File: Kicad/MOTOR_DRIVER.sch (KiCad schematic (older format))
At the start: 8 parts, among them J1 CONN_MOTOR, U1 SHFTREG_H, U2 LV8727

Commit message: 
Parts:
- removed L1: __BATTERYBARLUG, ~, symbol __BATTERYBARLUG
- added L1: LUG, ~, symbol LUG
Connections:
- net labels added: CS, FR, SDIN, SDOUT, STEP, VREF
- net labels removed: MOTOR_CS, MOTOR_FR, MOTOR_SDIN, MOTOR_SDOUT, MOTOR_STEP, MOTOR_VREF

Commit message: All wired. ERC passes with no errors. Might be good to go.
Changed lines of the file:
@@
 $Descr A4 11693 8268
 encoding utf-8
-Sheet 2 15
+Sheet 14 15
 Title ""
-Date "7 jun 2014"
+Date "8 jun 2014"
 Rev ""
 Comp ""
@@
 P 5650 2400
 AR Path="/5387F799/53880645" Ref="U2"  Part="1"
-AR Path="/5393B696/53880645" Ref="U12"  Part="1"
-AR Path="/5393E24C/53880645" Ref="U14"  Part="1"
-AR Path="/5393E5B4/53880645" Ref="U16"  Part="1"
-F 0 "U2" V 4300 2600 60  0000 C CNN
+AR Path="/5393B696/53880645" Ref="U8"  Part="1"
+AR Path="/5393E24C/53880645" Ref="U10"  Part="1"
+AR Path="/5393E5B4/53880645" Ref="U12"  Part="1"
+F 0 "U12" V 4300 2600 60  0000 C CNN
 F 1 "LV8727" V 7050 2600 60  0000 C CNN
 F 2 "~" H 5650 2400 60  0000 C CNN
@@
 P 4250 5150
 AR Path="/5387F799/53880692" Ref="U1"  Part="1"
-AR Path="/5393B696/53880692" Ref="U11"  Part="1"
-AR Path="/5393E24C/53880692" Ref="U13"  Part="1"
-AR Path="/5393E5B4/53880692" Ref="U15"  Part="1"
-F 0 "U1" H 4250 5700 60  0000 C CNN
+AR Path="/5393B696/53880692" Ref="U7"  Part="1"
+AR Path="/5393E24C/53880692" Ref="U9"  Part="1"
+AR Path="/5393E5B4/53880692" Ref="U11"  Part="1"
+F 0 "U11" H 4250 5700 60  0000 C CNN
 F 1 "SHFTREG_H" H 4250 4600 60  0000 C CNN
 F 2 "~" V 4000 5250 60  0000 C CNN
@@
 P 6750 2950
 AR Path="/5387F799/538A3F7A" Ref="R2"  Part="1"
-AR Path="/5393B696/538A3F7A" Ref="R16"  Part="1"
-AR Path="/5393E24C/538A3F7A" Ref="R18"  Part="1"
-AR Path="/5393E5B4/538A3F7A" Ref="R20"  Part="1"
-F 0 "R2" V 6830 2950 40  0000 C CNN
+AR Path="/5393B696/538A3F7A" Ref="R10"  Part="1"
+AR Path="/5393E24C/538A3F7A" Ref="R12"  Part="1"
+AR Path="/5393E5B4/538A3F7A" Ref="R14"  Part="1"
+F 0 "R14" V 6830 2950 40  0000 C CNN
 F 1 "0.1" V 6757 2951 40  0000 C CNN
 F 2 "~" V 6680 2950 30  0000 C CNN
@@
 P 4550 2950
 AR Path="/5387F799/538A3F87" Ref="R1"  Part="1"
-AR Path="/5393B696/538A3F87" Ref="R15"  Part="1"
-AR Path="/5393E24C/538A3F87" Ref="R17"  Part="1"
-AR Path="/5393E5B4/538A3F87" Ref="R19"  Part="1"
-F 0 "R1" V 4630 2950 40  0000 C CNN
+AR Path="/5393B696/538A3F87" Ref="R9"  Part="1"
+AR Path="/5393E24C/538A3F87" Ref="R11"  Part="1"
+AR Path="/5393E5B4/538A3F87" Ref="R13"  Part="1"
+F 0 "R13" V 4630 2950 40  0000 C CNN
 F 1 "0.1" V 4557 2951 40  0000 C CNN
 F 2 "~" V 4480 2950 30  0000 C CNN
@@
 AR Path="/5393E24C/538A3FA9" Ref="C5"  Part="1"
 AR Path="/5393E5B4/538A3FA9" Ref="C7"  Part="1"
-F 0 "C1" H 4850 4450 40  0000 L CNN
+F 0 "C7" H 4850 4450 40  0000 L CNN
 F 1 "1000u" H 4856 4265 40  0000 L CNN
 F 2 "~" H 4888 4200 30  0000 C CNN
@@
 P 4850 4600
 AR Path="/5387F799/538A3FB8" Ref="#PWR07"  Part="1"
-AR Path="/5393B696/538A3FB8" Ref="#PWR057"  Part="1"
-AR Path="/5393E24C/538A3FB8" Ref="#PWR066"  Part="1"
-AR Path="/5393E5B4/538A3FB8" Ref="#PWR075"  Part="1"
-F 0 "#PWR07" H 4850 4600 30  0001 C CNN
+AR Path="/5393B696/538A3FB8" Ref="#PWR050"  Part="1"
+AR Path="/5393E24C/538A3FB8" Ref="#PWR059"  Part="1"
+AR Path="/5393E5B4/538A3FB8" Ref="#PWR068"  Part="1"
+F 0 "#PWR068" H 4850 4600 30  0001 C CNN
 F 1 "GND" H 4850 4530 30  0001 C CNN
 F 2 "" H 4850 4600 60  0000 C CNN
@@
 P 6350 2750
 AR Path="/5387F799/538A3FEF" Ref="#PWR08"  Part="1"
-AR Path="/5393B696/538A3FEF" Ref="#PWR058"  Part="1"
-AR Path="/5393E24C/538A3FEF" Ref="#PWR067"  Part="1"
-AR Path="/5393E5B4/538A3FEF" Ref="#PWR076"  Part="1"
-F 0 "#PWR08" H 6350 2750 30  0001 C CNN
+AR Path="/5393B696/538A3FEF" Ref="#PWR051"  Part="1"
+AR Path="/5393E24C/538A3FEF" Ref="#PWR060"  Part="1"
+AR Path="/5393E5B4/538A3FEF" Ref="#PWR069"  Part="1"
+F 0 "#PWR069" H 6350 2750 30  0001 C CNN
 F 1 "GND" H 6350 2680 30  0001 C CNN
 F 2 "" H 6350 2750 60  0000 C CNN
@@
 P 6650 2750
 AR Path="/5387F799/538A3FF5" Ref="#PWR09"  Part="1"
-AR Path="/5393B696/538A3FF5" Ref="#PWR059"  Part="1"
-AR Path="/5393E24C/538A3FF5" Ref="#PWR068"  Part="1"
-AR Path="/5393E5B4/538A3FF5" Ref="#PWR077"  Part="1"
-F 0 "#PWR09" H 6650 2750 30  0001 C CNN
+AR Path="/5393B696/538A3FF5" Ref="#PWR052"  Part="1"
+AR Path="/5393E24C/538A3FF5" Ref="#PWR061"  Part="1"
+AR Path="/5393E5B4/538A3FF5" Ref="#PWR070"  Part="1"
+F 0 "#PWR070" H 6650 2750 30  0001 C CNN
 F 1 "GND" H 6650 2680 30  0001 C CNN
 F 2 "" H 6650 2750 60  0000 C CNN
@@
 P 4650 2750
 AR Path="/5387F799/538A3FFB" Ref="#PWR010"  Part="1"
-AR Path="/5393B696/538A3FFB" Ref="#PWR060"  Part="1"
-AR Path="/5393E24C/538A3FFB" Ref="#PWR069"  Part="1"
-AR Path="/5393E5B4/538A3FFB" Ref="#PWR078"  Part="1"
-F 0 "#PWR010" H 4650 2750 30  0001 C CNN
+AR Path="/5393B696/538A3FFB" Ref="#PWR053"  Part="1"
+AR Path="/5393E24C/538A3FFB" Ref="#PWR062"  Part="1"
+AR Path="/5393E5B4/538A3FFB" Ref="#PWR071"  Part="1"
+F 0 "#PWR071" H 4650 2750 30  0001 C CNN
 F 1 "GND" H 4650 2680 30  0001 C CNN
 F 2 "" H 4650 2750 60  0000 C CNN
@@
 P 4550 3250
 AR Path="/5387F799/538A4FB3" Ref="#PWR011"  Part="1"
-AR Path="/5393B696/538A4FB3" Ref="#PWR061"  Part="1"
-AR Path="/5393E24C/538A4FB3" Ref="#PWR070"  Part="1"
-AR Path="/5393E5B4/538A4FB3" Ref="#PWR079"  Part="1"
-F 0 "#PWR011" H 4550 3250 30  0001 C CNN
+AR Path="/5393B696/538A4FB3" Ref="#PWR054"  Part="1"
+AR Path="/5393E24C/538A4FB3" Ref="#PWR063"  Part="1"
+AR Path="/5393E5B4/538A4FB3" Ref="#PWR072"  Part="1"
+F 0 "#PWR072" H 4550 3250 30  0001 C CNN
 F 1 "GND" H 4550 3180 30  0001 C CNN
 F 2 "" H 4550 3250 60  0000 C CNN
@@
 P 6750 3250
 AR Path="/5387F799/538A4FB9" Ref="#PWR012"  Part="1"
-AR Path="/5393B696/538A4FB9" Ref="#PWR062"  Part="1"
-AR Path="/5393E24C/538A4FB9" Ref="#PWR071"  Part="1"
-AR Path="/5393E5B4/538A4FB9" Ref="#PWR080"  Part="1"
-F 0 "#PWR012" H 6750 3250 30  0001 C CNN
+AR Path="/5393B696/538A4FB9" Ref="#PWR055"  Part="1"
+AR Path="/5393E24C/538A4FB9" Ref="#PWR064"  Part="1"
+AR Path="/5393E5B4/538A4FB9" Ref="#PWR073"  Part="1"
+F 0 "#PWR073" H 6750 3250 30  0001 C CNN
 F 1 "GND" H 6750 3180 30  0001 C CNN
 F 2 "" H 6750 3250 60  0000 C CNN
@@
 AR Path="/5393E24C/538A522E" Ref="C6"  Part="1"
 AR Path="/5393E5B4/538A522E" Ref="C8"  Part="1"
-F 0 "C2" H 5800 3100 40  0000 L CNN
+F 0 "C8" H 5800 3100 40  0000 L CNN
 F 1 "180p" H 5806 2915 40  0000 L CNN
 F 2 "~" H 5838 2850 30  0000 C CNN
@@
 P 5800 3250
 AR Path="/5387F799/538A5251" Ref="#PWR013"  Part="1"
-AR Path="/5393B696/538A5251" Ref="#PWR063"  Part="1"
-AR Path="/5393E24C/538A5251" Ref="#PWR072"  Part="1"
-AR Path="/5393E5B4/538A5251" Ref="#PWR081"  Part="1"
-F 0 "#PWR013" H 5800 3250 30  0001 C CNN
+AR Path="/5393B696/538A5251" Ref="#PWR056"  Part="1"
+AR Path="/5393E24C/538A5251" Ref="#PWR065"  Part="1"
+AR Path="/5393E5B4/538A5251" Ref="#PWR074"  Part="1"
+F 0 "#PWR074" H 5800 3250 30  0001 C CNN
 F 1 "GND" H 5800 3180 30  0001 C CNN
 F 2 "" H 5800 3250 60  0000 C CNN
@@
 P 5850 1200
 AR Path="/5387F799/538A7481" Ref="J1"  Part="1"
-AR Path="/5393B696/538A7481" Ref="J14"  Part="1"
-AR Path="/5393E24C/538A7481" Ref="J15"  Part="1"
-AR Path="/5393E5B4/538A7481" Ref="J16"  Part="1"
-F 0 "J1" H 5850 1350 60  0000 C CNN
+AR Path="/5393B696/538A7481" Ref="J12"  Part="1"
+AR Path="/5393E24C/538A7481" Ref="J13"  Part="1"
+AR Path="/5393E5B4/538A7481" Ref="J14"  Part="1"
+F 0 "J14" H 5850 1350 60  0000 C CNN
 F 1 "CONN_MOTOR" H 6350 1200 60  0000 C CNN
 F 2 "~" H 5700 1150 60  0000 C CNN
@@
 P 3650 4750
 AR Path="/5387F799/538A78DB" Ref="#PWR014"  Part="1"
-AR Path="/5393B696/538A78DB" Ref="#PWR064"  Part="1"
-AR Path="/5393E24C/538A78DB" Ref="#PWR073"  Part="1"
-AR Path="/5393E5B4/538A78DB" Ref="#PWR082"  Part="1"
-F 0 "#PWR014" H 3650 4710 30  0001 C CNN
+AR Path="/5393B696/538A78DB" Ref="#PWR057"  Part="1"
+AR Path="/5393E24C/538A78DB" Ref="#PWR066"  Part="1"
+AR Path="/5393E5B4/538A78DB" Ref="#PWR075"  Part="1"
+F 0 "#PWR075" H 3650 4710 30  0001 C CNN
 F 1 "+3.3V" H 3650 4860 30  0000 C CNN
 F 2 "" H 3650 4750 60  0000 C CNN
@@
 P 3650 5600
 AR Path="/5387F799/538A7924" Ref="#PWR015"  Part="1"
-AR Path="/5393B696/538A7924" Ref="#PWR065"  Part="1"
-AR Path="/5393E24C/538A7924" Ref="#PWR074"  Part="1"
-AR Path="/5393E5B4/538A7924" Ref="#PWR083"  Part="1"
-F 0 "#PWR015" H 3650 5600 30  0001 C CNN
+AR Path="/5393B696/538A7924" Ref="#PWR058"  Part="1"
+AR Path="/5393E24C/538A7924" Ref="#PWR067"  Part="1"
+AR Path="/5393E5B4/538A7924" Ref="#PWR076"  Part="1"
+F 0 "#PWR076" H 3650 5600 30  0001 C CNN
 F 1 "GND" H 3650 5530 30  0001 C CNN
 F 2 "" H 3650 5600 60  0000 C CNN
@@
 AR Path="/5393E24C/538B71FB" Ref="L9"  Part="1"
 AR Path="/5393E5B4/538B71FB" Ref="L10"  Part="1"
-F 0 "L1" H 4750 3600 60  0000 C CNN
+F 0 "L10" H 4750 3600 60  0000 C CNN
 F 1 "LUG" H 4650 3700 20  0000 C CNN
 F 2 "~" H 4550 3550 60  0000 C CNN

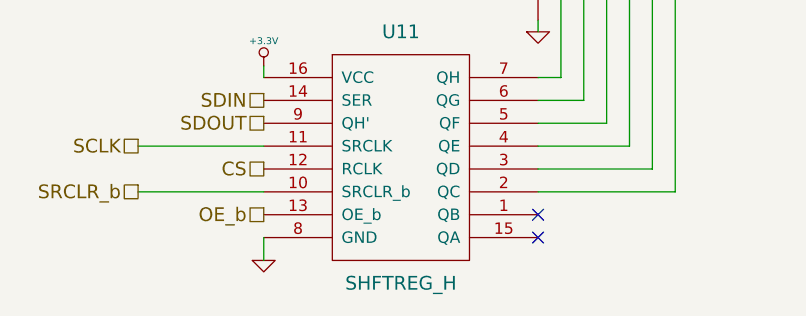
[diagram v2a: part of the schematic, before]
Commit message: 
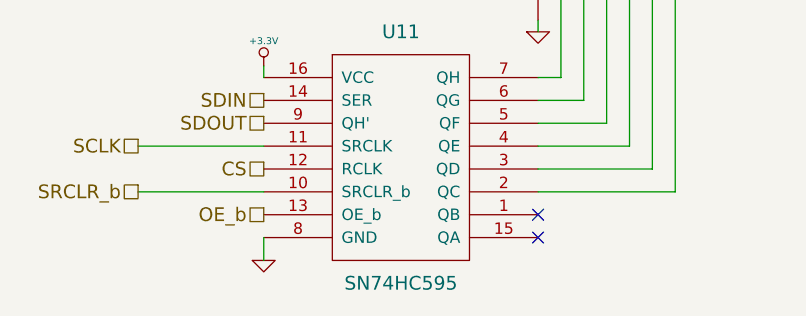
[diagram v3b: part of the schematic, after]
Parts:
- U1: value SHFTREG_H -> SN74HC595
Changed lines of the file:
@@
 AR Path="/5393E5B4/53880692" Ref="U11"  Part="1"
 F 0 "U11" H 4250 5700 60  0000 C CNN
-F 1 "SHFTREG_H" H 4250 4600 60  0000 C CNN
+F 1 "SN74HC595" H 4250 4600 60  0000 C CNN
 F 2 "~" V 4000 5250 60  0000 C CNN
 F 3 "~" V 4000 5250 60  0000 C CNN

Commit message: 
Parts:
- removed C1: 1000u, ~, symbol C
- added C1: 1000u, ~, symbol CAPAPOL
- R1, R2: value 0.1 -> 0.27
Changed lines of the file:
@@
 LIBS:contrib
 LIBS:valves
-LIBS:___power_diode
-LIBS:__batterybarlug
-LIBS:__freedom_x
-LIBS:__xbee-pro
-LIBS:CAR
 LIBS:car_v3-cache
 EELAYER 27 0
@@
 $Descr A4 11693 8268
 encoding utf-8
-Sheet 14 15
+Sheet 2 15
 Title ""
-Date "8 jun 2014"
+Date "13 jul 2014"
 Rev ""
 Comp ""
@@
 AR Path="/5393E24C/53880645" Ref="U10"  Part="1"
 AR Path="/5393E5B4/53880645" Ref="U12"  Part="1"
-F 0 "U12" V 4300 2600 60  0000 C CNN
+F 0 "U2" V 4300 2600 60  0000 C CNN
 F 1 "LV8727" V 7050 2600 60  0000 C CNN
 F 2 "~" H 5650 2400 60  0000 C CNN
@@
 AR Path="/5393E24C/53880692" Ref="U9"  Part="1"
 AR Path="/5393E5B4/53880692" Ref="U11"  Part="1"
-F 0 "U11" H 4250 5700 60  0000 C CNN
+F 0 "U1" H 4250 5700 60  0000 C CNN
 F 1 "SN74HC595" H 4250 4600 60  0000 C CNN
 F 2 "~" V 4000 5250 60  0000 C CNN
@@
 AR Path="/5393E24C/538A3F7A" Ref="R12"  Part="1"
 AR Path="/5393E5B4/538A3F7A" Ref="R14"  Part="1"
-F 0 "R14" V 6830 2950 40  0000 C CNN
-F 1 "0.1" V 6757 2951 40  0000 C CNN
+F 0 "R2" V 6830 2950 40  0000 C CNN
+F 1 "0.27" V 6757 2951 40  0000 C CNN
 F 2 "~" V 6680 2950 30  0000 C CNN
 F 3 "~" H 6750 2950 30  0000 C CNN
@@
 AR Path="/5393E24C/538A3F87" Ref="R11"  Part="1"
 AR Path="/5393E5B4/538A3F87" Ref="R13"  Part="1"
-F 0 "R13" V 4630 2950 40  0000 C CNN
-F 1 "0.1" V 4557 2951 40  0000 C CNN
+F 0 "R1" V 4630 2950 40  0000 C CNN
+F 1 "0.27" V 4557 2951 40  0000 C CNN
 F 2 "~" V 4480 2950 30  0000 C CNN
 F 3 "~" H 4550 2950 30  0000 C CNN
 	1    4550 2950
-	1    0    0    -1
-$EndComp
-$Comp
-L C C1
-U 1 1 538A3FA9
-P 4850 4350
-AR Path="/5387F799/538A3FA9" Ref="C1"  Part="1"
-AR Path="/5393B696/538A3FA9" Ref="C3"  Part="1"
-AR Path="/5393E24C/538A3FA9" Ref="C5"  Part="1"
-AR Path="/5393E5B4/538A3FA9" Ref="C7"  Part="1"
-F 0 "C7" H 4850 4450 40  0000 L CNN
-F 1 "1000u" H 4856 4265 40  0000 L CNN
-F 2 "~" H 4888 4200 30  0000 C CNN
-F 3 "~" H 4850 4350 60  0000 C CNN
-	1    4850 4350
 	1    0    0    -1
 $EndComp
@@
 AR Path="/5393E24C/538A3FB8" Ref="#PWR059"  Part="1"
 AR Path="/5393E5B4/538A3FB8" Ref="#PWR068"  Part="1"
-F 0 "#PWR068" H 4850 4600 30  0001 C CNN
+F 0 "#PWR07" H 4850 4600 30  0001 C CNN
 F 1 "GND" H 4850 4530 30  0001 C CNN
 F 2 "" H 4850 4600 60  0000 C CNN
@@
 AR Path="/5393E24C/538A3FEF" Ref="#PWR060"  Part="1"
 AR Path="/5393E5B4/538A3FEF" Ref="#PWR069"  Part="1"
-F 0 "#PWR069" H 6350 2750 30  0001 C CNN
+F 0 "#PWR08" H 6350 2750 30  0001 C CNN
 F 1 "GND" H 6350 2680 30  0001 C CNN
 F 2 "" H 6350 2750 60  0000 C CNN
@@
 AR Path="/5393E24C/538A3FF5" Ref="#PWR061"  Part="1"
 AR Path="/5393E5B4/538A3FF5" Ref="#PWR070"  Part="1"
-F 0 "#PWR070" H 6650 2750 30  0001 C CNN
+F 0 "#PWR09" H 6650 2750 30  0001 C CNN
 F 1 "GND" H 6650 2680 30  0001 C CNN
 F 2 "" H 6650 2750 60  0000 C CNN
@@
 AR Path="/5393E24C/538A3FFB" Ref="#PWR062"  Part="1"
 AR Path="/5393E5B4/538A3FFB" Ref="#PWR071"  Part="1"
-F 0 "#PWR071" H 4650 2750 30  0001 C CNN
+F 0 "#PWR010" H 4650 2750 30  0001 C CNN
 F 1 "GND" H 4650 2680 30  0001 C CNN
 F 2 "" H 4650 2750 60  0000 C CNN
@@
 AR Path="/5393E24C/538A4FB3" Ref="#PWR063"  Part="1"
 AR Path="/5393E5B4/538A4FB3" Ref="#PWR072"  Part="1"
-F 0 "#PWR072" H 4550 3250 30  0001 C CNN
+F 0 "#PWR011" H 4550 3250 30  0001 C CNN
 F 1 "GND" H 4550 3180 30  0001 C CNN
 F 2 "" H 4550 3250 60  0000 C CNN
@@
 AR Path="/5393E24C/538A4FB9" Ref="#PWR064"  Part="1"
 AR Path="/5393E5B4/538A4FB9" Ref="#PWR073"  Part="1"
-F 0 "#PWR073" H 6750 3250 30  0001 C CNN
+F 0 "#PWR012" H 6750 3250 30  0001 C CNN
 F 1 "GND" H 6750 3180 30  0001 C CNN
 F 2 "" H 6750 3250 60  0000 C CNN
@@
 Wire Wire Line
 	6250 2700 6250 2800
-$Comp
-L C C2
-U 1 1 538A522E
-P 5800 3000
-AR Path="/5387F799/538A522E" Ref="C2"  Part="1"
-AR Path="/5393B696/538A522E" Ref="C4"  Part="1"
-AR Path="/5393E24C/538A522E" Ref="C6"  Part="1"
-AR Path="/5393E5B4/538A522E" Ref="C8"  Part="1"
-F 0 "C8" H 5800 3100 40  0000 L CNN
-F 1 "180p" H 5806 2915 40  0000 L CNN
-F 2 "~" H 5838 2850 30  0000 C CNN
-F 3 "~" H 5800 3000 60  0000 C CNN
-	1    5800 3000
-	1    0    0    -1
-$EndComp
 Wire Wire Line
 	5750 2700 5750 2800
@@
 AR Path="/5393E24C/538A5251" Ref="#PWR065"  Part="1"
 AR Path="/5393E5B4/538A5251" Ref="#PWR074"  Part="1"
-F 0 "#PWR074" H 5800 3250 30  0001 C CNN
+F 0 "#PWR013" H 5800 3250 30  0001 C CNN
 F 1 "GND" H 5800 3180 30  0001 C CNN
 F 2 "" H 5800 3250 60  0000 C CNN
@@
 AR Path="/5393E24C/538A7481" Ref="J13"  Part="1"
 AR Path="/5393E5B4/538A7481" Ref="J14"  Part="1"
-F 0 "J14" H 5850 1350 60  0000 C CNN
+F 0 "J1" H 5850 1350 60  0000 C CNN
 F 1 "CONN_MOTOR" H 6350 1200 60  0000 C CNN
 F 2 "~" H 5700 1150 60  0000 C CNN
@@
 AR Path="/5393E24C/538A78DB" Ref="#PWR066"  Part="1"
 AR Path="/5393E5B4/538A78DB" Ref="#PWR075"  Part="1"
-F 0 "#PWR075" H 3650 4710 30  0001 C CNN
+F 0 "#PWR014" H 3650 4710 30  0001 C CNN
 F 1 "+3.3V" H 3650 4860 30  0000 C CNN
 F 2 "" H 3650 4750 60  0000 C CNN
@@
 AR Path="/5393E24C/538A7924" Ref="#PWR067"  Part="1"
 AR Path="/5393E5B4/538A7924" Ref="#PWR076"  Part="1"
-F 0 "#PWR076" H 3650 5600 30  0001 C CNN
+F 0 "#PWR015" H 3650 5600 30  0001 C CNN
 F 1 "GND" H 3650 5530 30  0001 C CNN
 F 2 "" H 3650 5600 60  0000 C CNN
@@
 AR Path="/5393E24C/538B71FB" Ref="L9"  Part="1"
 AR Path="/5393E5B4/538B71FB" Ref="L10"  Part="1"
-F 0 "L10" H 4750 3600 60  0000 C CNN
+F 0 "L1" H 4750 3600 60  0000 C CNN
 F 1 "LUG" H 4650 3700 20  0000 C CNN
 F 2 "~" H 4550 3550 60  0000 C CNN
@@
 Text HLabel 3650 5400 0    60   UnSpc ~ 0
 OE_b
+$Comp
+L CAPAPOL C1
+U 1 1 53B73F47
+P 4850 4350
+AR Path="/5387F799/53B73F47" Ref="C1"  Part="1"
+AR Path="/5393B696/53B73F47" Ref="C3"  Part="1"
+AR Path="/5393E24C/53B73F47" Ref="C5"  Part="1"
+AR Path="/5393E5B4/53B73F47" Ref="C7"  Part="1"
+F 0 "C1" H 4900 4450 40  0000 L CNN
+F 1 "1000u" H 4900 4250 40  0000 L CNN
+F 2 "~" H 4950 4200 30  0000 C CNN
+F 3 "~" H 4850 4350 300 0000 C CNN
+	1    4850 4350
+	1    0    0    -1
+$EndComp
+$Comp
+L C C2
+U 1 1 53B746FA
+P 5800 3000
+AR Path="/5387F799/53B746FA" Ref="C2"  Part="1"
+AR Path="/5393B696/53B746FA" Ref="C4"  Part="1"
+AR Path="/5393E24C/53B746FA" Ref="C6"  Part="1"
+AR Path="/5393E5B4/53B746FA" Ref="C8"  Part="1"
+F 0 "C2" H 5800 3100 40  0000 L CNN
+F 1 "180p" H 5806 2915 40  0000 L CNN
+F 2 "~" H 5838 2850 30  0000 C CNN
+F 3 "~" H 5800 3000 60  0000 C CNN
+	1    5800 3000
+	1    0    0    -1
+$EndComp
 $EndSCHEMATC
